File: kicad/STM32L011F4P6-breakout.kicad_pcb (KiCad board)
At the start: 2 copper layers, 17 x 26.9 mm, 13 parts

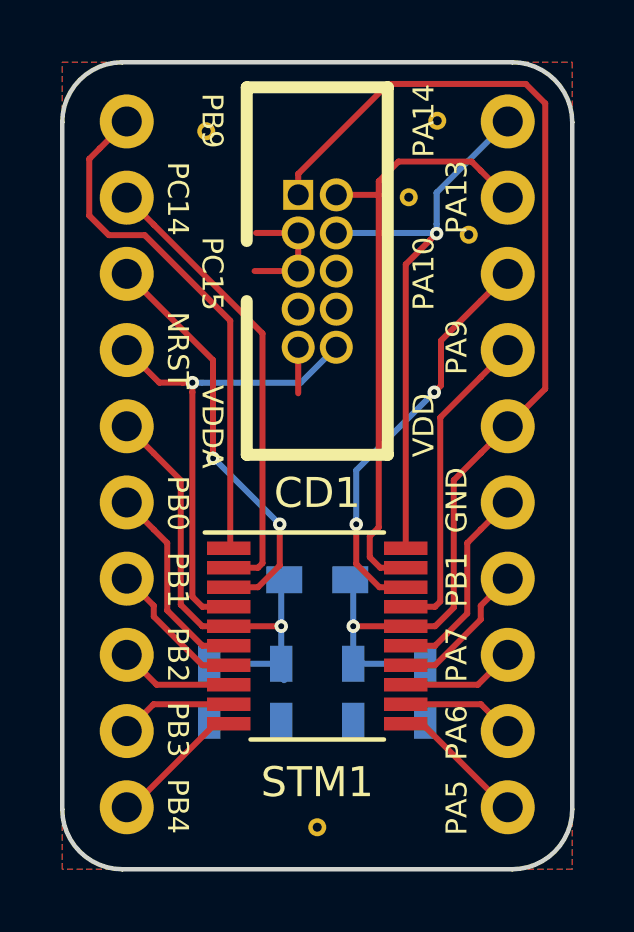
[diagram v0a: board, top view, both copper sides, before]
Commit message: changed ferrite bead
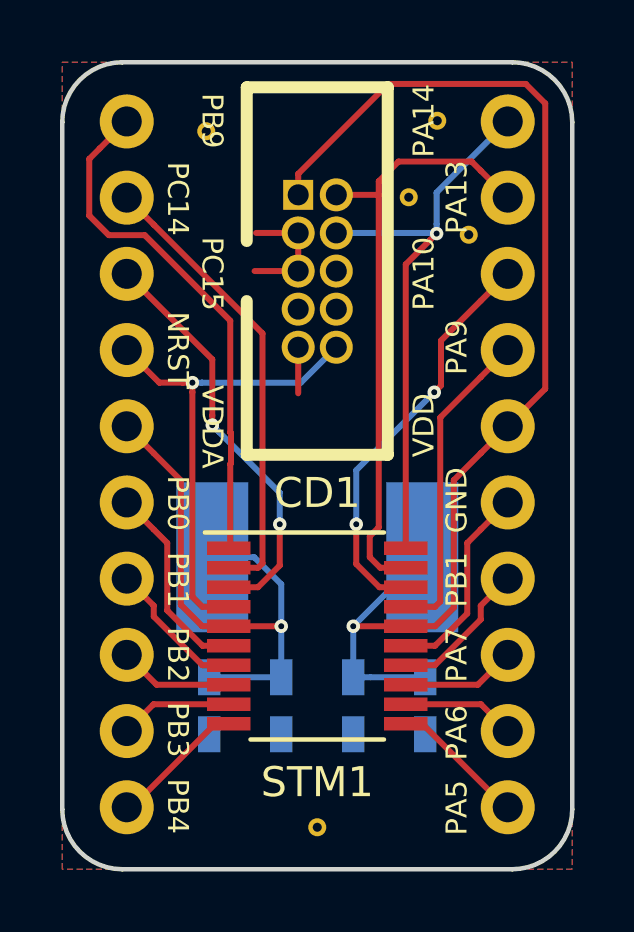
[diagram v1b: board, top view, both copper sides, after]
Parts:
- L1: value BKP1608HS600-T -> NFZ5BBW100LN10L; footprint Resistors_SMD:R_0603_HandSoldering -> Capacitors_SMD:C_2220_HandSoldering
- moved L1 0.75 mm to (148.5, 108.1)
- moved C1 0.45 mm to (144.9, 113.0)
- moved C2 0.45 mm to (147.3, 113.0)
- moved C3 0.45 mm to (149.7, 113.0)
- moved C4 0.45 mm to (152.1, 113.0)
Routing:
- net Net-(C3-Pad1): track 37.3 -> 40.3 mm
- net Net-(C1-Pad1): track 16.0 -> 18.9 mm
